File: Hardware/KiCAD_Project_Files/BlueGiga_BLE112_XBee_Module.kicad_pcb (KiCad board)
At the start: 4 copper layers, 24.5 x 24.4 mm, 11 parts, among them J2 HEADER_F_XBEE_PTH, P1 HEADER_2X5, U1 BLE112-A, U2 AAT3221

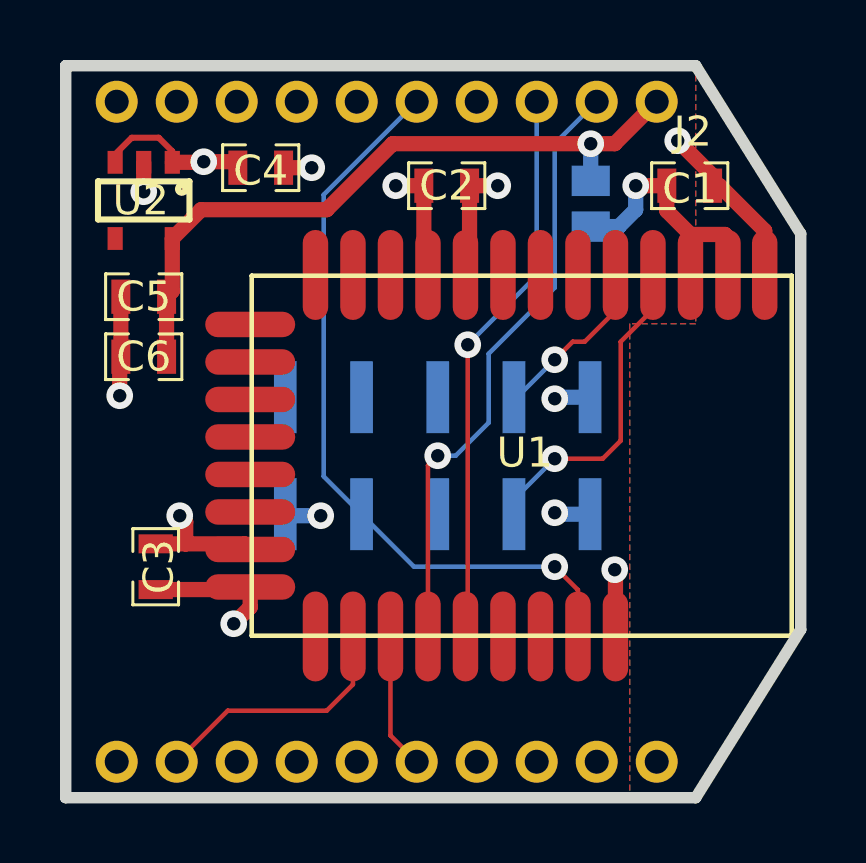
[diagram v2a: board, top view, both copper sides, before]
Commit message: Updated PCB layout to put 2mm pin header at same location as the RN-41XV. Added silkscreen artwork to back of PCB. Added assembly pdf drawings and schematic pdf. Added OSH Park PCB render images.
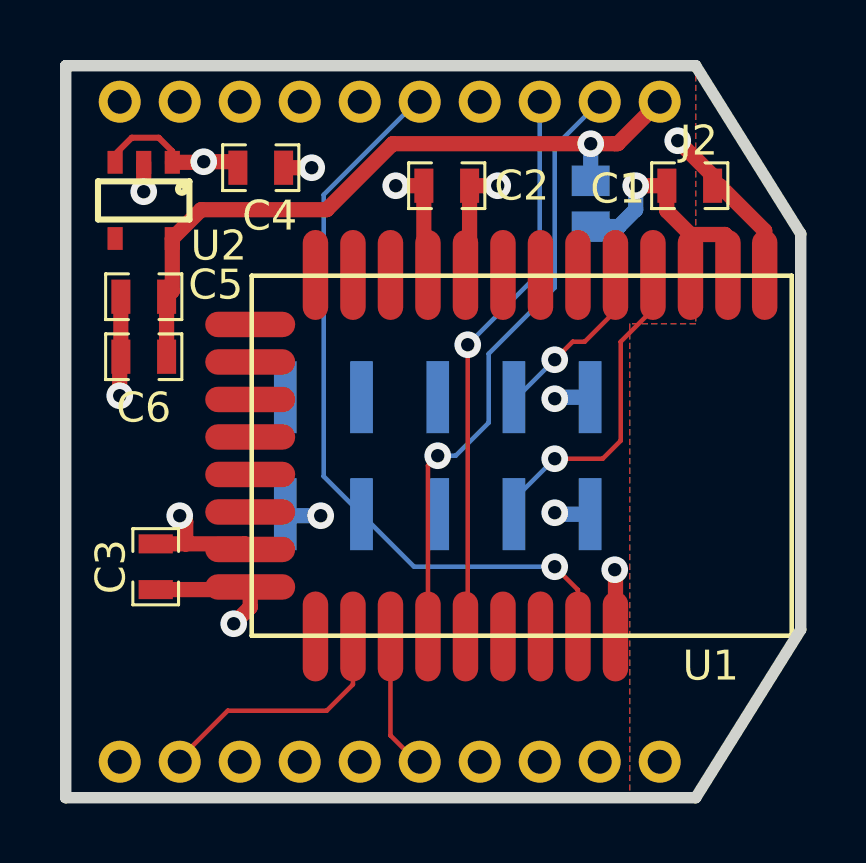
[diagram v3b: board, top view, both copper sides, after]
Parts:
- P1: value HEADER_2X5 -> (none)
- moved J2 0.10 mm to (118.8, 92.8)
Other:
- board text added: "BLE112"
- board text added: "REV 1"
- board text added: "www.cascologix.com"
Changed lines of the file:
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@@
     (links 36)
     (no_connects 0)
-    (area 85.517999 72.8948 126.3324 105.190501)
+    (area 98.809499 80.409499 123.690501 105.190501)
     (thickness 1.6002)
-    (drawings 8)
-    (tracks 124)
+    (drawings 11)
+    (tracks 128)
     (zones 0)
     (modules 11)
@@
   (module BLE112 locked (layer Front)
     (at 114.2 93.6 270)
-    (fp_text reference U1 (at -0.1 -0.1 360) (layer F.SilkS)
+    (fp_text reference U1 (at 7 -6.3 360) (layer F.SilkS)
       (effects (font (size 1 1) (thickness 0.1)))
     )
@@
     (at 119.8 84.6)
     (attr smd)
-    (fp_text reference C1 (at 0 0.1) (layer F.SilkS)
+    (fp_text reference C1 (at -2.4 0.1) (layer F.SilkS)
       (effects (font (size 1 1) (thickness 0.1)))
     )
@@
     (at 111.7 84.6 180)
     (attr smd)
-    (fp_text reference C2 (at 0 0 180) (layer F.SilkS)
+    (fp_text reference C2 (at -2.5 0 180) (layer F.SilkS)
       (effects (font (size 1 1) (thickness 0.1)))
     )
@@
     (at 102 97.3 270)
     (attr smd)
-    (fp_text reference C3 (at 0 -0.1 270) (layer F.SilkS)
+    (fp_text reference C3 (at 0 1.5 270) (layer F.SilkS)
       (effects (font (size 1 1) (thickness 0.1)))
     )
@@
     (at 105.5 84)
     (attr smd)
-    (fp_text reference C4 (at 0 0.1) (layer F.SilkS)
+    (fp_text reference C4 (at 0.3 1.6) (layer F.SilkS)
       (effects (font (size 1 1) (thickness 0.1)))
     )
@@
     (at 101.6 88.3 180)
     (attr smd)
-    (fp_text reference C5 (at 0 0 180) (layer F.SilkS)
+    (fp_text reference C5 (at -2.4 0.4 180) (layer F.SilkS)
       (effects (font (size 1 1) (thickness 0.1)))
     )
@@
     (at 101.6 90.3 180)
     (attr smd)
-    (fp_text reference C6 (at 0 0 180) (layer F.SilkS)
+    (fp_text reference C6 (at 0 -1.7 180) (layer F.SilkS)
       (effects (font (size 1 1) (thickness 0.1)))
     )
@@
   (module SOLDER_LINK (layer Back)
     (at 116.5 85.2)
-    (fp_text reference LK1 (at 0 0 270) (layer B.SilkS)
+    (fp_text reference LK1 (at -1.7 0 270) (layer B.SilkS)
       (effects (font (size 1 1) (thickness 0.1)) (justify mirror))
     )
@@
     (at 101.6 85.09 270)
     (attr smd)
-    (fp_text reference U2 (at 0 0.1 360) (layer F.SilkS)
+    (fp_text reference U2 (at 1.51 -2.5 360) (layer F.SilkS)
       (effects (font (size 1 1) (thickness 0.1)))
     )
@@
     )
   )
-  (module HEADER_XBEE locked (layer Front)
-    (at 118.7 92.8 270)
-    (fp_text reference J2 (at -10 -1.2 360) (layer F.SilkS)
+  (module HEADER_XBEE (layer Front)
+    (at 118.8 92.8 270)
+    (fp_text reference J2 (at -9.7 -1.3 540) (layer F.SilkS)
       (effects (font (size 1 1) (thickness 0.1)))
     )
@@
       (effects (font (size 1.016 1.016) (thickness 0.1524)) (justify mirror))
     )
-    (fp_text value HEADER_2X5 (at 0 5.08 180) (layer B.SilkS)
+    (fp_text value "" (at 0 5.08 180) (layer B.SilkS) hide
       (effects (font (size 1.016 1.016) (thickness 0.1524)) (justify mirror))
     )
@@
       (layers Back B.Paste B.Mask)
     )
+  )
+  (gr_text "REV 1" (at 101.3 93.1 270) (layer B.SilkS)
+    (effects (font (size 2.032 1.524) (thickness 0.3048)) (justify mirror))
+  )
+  (gr_text BLE112 (at 104.1 84.7) (layer B.SilkS)
+    (effects (font (size 2.032 1.524) (thickness 0.3048)) (justify mirror))
+  )
+  (gr_text www.cascologix.com (at 111.2 87.7) (layer B.SilkS)
+    (effects (font (size 2.032 1.524) (thickness 0.3048)) (justify mirror))
   )
   (dimension 24.4 (width 0.3048) (layer Dwgs.User)
@@
   (segment (start 112.462 87.438) (end 112.325 87.575) (width 0.508) (layer Front) (net 1))
   (segment (start 119.825 87.575) (end 119.825 86.225) (width 0.508) (layer Front) (net 1))
-  (segment (start 109.825 99.625) (end 109.825 102.925) (width 0.1524) (layer Front) (net 2))
-  (segment (start 109.825 102.925) (end 110.7 103.8) (width 0.1524) (layer Front) (net 2))
+  (segment (start 110.8 103.8) (end 110.7 103.8) (width 0.1524) (layer Front) (net 2))
+  (segment (start 109.825 102.925) (end 109.825 99.625) (width 0.1524) (layer Front) (net 2))
+  (segment (start 110.7 103.8) (end 109.825 102.925) (width 0.1524) (layer Front) (net 2))
   (segment (start 116.48 95.55) (end 115.35 95.55) (width 0.508) (layer Back) (net 3))
   (via (at 115.3 95.5) (size 0.889) (layers Front Back) (net 3))
@@
   (segment (start 117.5 93.1) (end 117.5 89.8) (width 0.1524) (layer Front) (net 5))
   (segment (start 116.9 93.7) (end 117.5 93.1) (width 0.1524) (layer Front) (net 5))
+  (segment (start 110.8 81.8) (end 110.7 81.8) (width 0.1524) (layer Back) (net 6))
+  (segment (start 107.6 94.29) (end 108.86 95.55) (width 0.1524) (layer Back) (net 6))
+  (segment (start 107.6 84.9) (end 107.6 94.29) (width 0.1524) (layer Back) (net 6))
+  (segment (start 110.7 81.8) (end 107.6 84.9) (width 0.1524) (layer Back) (net 6))
   (segment (start 108.86 95.55) (end 110.61 97.3) (width 0.1524) (layer Back) (net 6))
   (segment (start 116.075 98.075) (end 116.075 99.625) (width 0.1524) (layer Front) (net 6))
@@
   (via (at 115.3 97.3) (size 0.889) (layers Front Back) (net 6))
   (segment (start 110.61 97.3) (end 115.3 97.3) (width 0.1524) (layer Back) (net 6))
-  (segment (start 110.7 81.8) (end 107.6 84.9) (width 0.1524) (layer Back) (net 6))
-  (segment (start 107.6 94.29) (end 108.86 95.55) (width 0.1524) (layer Back) (net 6))
-  (segment (start 107.6 84.9) (end 107.6 94.29) (width 0.1524) (layer Back) (net 6))
   (segment (start 108.86 95.55) (end 108.95 95.55) (width 0.1524) (layer Back) (net 6))
-  (segment (start 108.575 99.625) (end 108.575 101.225) (width 0.1524) (layer Front) (net 7))
-  (segment (start 104.4 102.1) (end 102.7 103.8) (width 0.1524) (layer Front) (net 7))
+  (segment (start 102.8 103.8) (end 102.8 103.7) (width 0.1524) (layer Front) (net 7))
+  (segment (start 108.575 101.225) (end 107.7 102.1) (width 0.1524) (layer Front) (net 7))
   (segment (start 107.7 102.1) (end 104.4 102.1) (width 0.1524) (layer Front) (net 7))
-  (segment (start 108.575 101.225) (end 107.7 102.1) (width 0.1524) (layer Front) (net 7))
+  (segment (start 108.575 101.225) (end 108.575 99.625) (width 0.1524) (layer Front) (net 7))
+  (segment (start 102.8 103.7) (end 104.4 102.1) (width 0.1524) (layer Front) (net 7))
+  (segment (start 114.7 87.6) (end 114.8 87.5) (width 0.1524) (layer Back) (net 8))
+  (segment (start 112.325 99.625) (end 112.4 99.55) (width 0.1524) (layer Front) (net 8))
+  (segment (start 112.4 89.9) (end 112.4 99.55) (width 0.1524) (layer Front) (net 8))
+  (via (at 112.4 89.9) (size 0.889) (layers Front Back) (net 8))
   (segment (start 112.4 89.9) (end 114.7 87.6) (width 0.1524) (layer Back) (net 8))
-  (via (at 112.4 89.9) (size 0.889) (layers Front Back) (net 8))
-  (segment (start 112.4 89.9) (end 112.4 99.55) (width 0.1524) (layer Front) (net 8))
-  (segment (start 112.325 99.625) (end 112.4 99.55) (width 0.1524) (layer Front) (net 8))
-  (segment (start 114.7 87.6) (end 114.7 81.8) (width 0.1524) (layer Back) (net 8))
+  (segment (start 114.8 87.5) (end 114.8 81.8) (width 0.1524) (layer Back) (net 8))
+  (segment (start 116.8 81.8) (end 115.3 83.3) (width 0.1524) (layer Back) (net 9))
   (segment (start 115.3 88) (end 113.1 90.2) (width 0.1524) (layer Back) (net 9))
-  (segment (start 116.7 81.8) (end 115.3 83.2) (width 0.1524) (layer Back) (net 9))
-  (segment (start 115.3 83.2) (end 115.3 88) (width 0.1524) (layer Back) (net 9))
+  (segment (start 115.3 83.3) (end 115.3 88) (width 0.1524) (layer Back) (net 9))
   (segment (start 111.075 93.925) (end 111.075 99.625) (width 0.1524) (layer Front) (net 9))
   (segment (start 111.4 93.6) (end 111.075 93.925) (width 0.1524) (layer Front) (net 9))
@@
   (segment (start 113.1 92.5) (end 112 93.6) (width 0.1524) (layer Back) (net 9))
   (segment (start 113.1 90.2) (end 113.1 92.5) (width 0.1524) (layer Back) (net 9))
+  (segment (start 118.8 81.8) (end 117.4 83.2) (width 0.508) (layer Front) (net 10))
+  (segment (start 117.3 83.2) (end 116.5 83.2) (width 0.508) (layer Front) (net 10))
+  (segment (start 117.3 83.2) (end 117.4 83.2) (width 0.508) (layer Front) (net 10))
   (segment (start 116.5 84.438) (end 116.5 83.2) (width 0.508) (layer Back) (net 10))
   (via (at 116.5 83.2) (size 0.889) (layers Front Back) (net 10))
-  (segment (start 118.7 81.8) (end 118.7 81.8) (width 0.508) (layer Front) (net 10))
   (segment (start 103.5125 85.4) (end 102.5525 86.36) (width 0.508) (layer Front) (net 10))
   (segment (start 107.7 85.4) (end 103.5125 85.4) (width 0.508) (layer Front) (net 10))
   (segment (start 109.9 83.2) (end 107.7 85.4) (width 0.508) (layer Front) (net 10))
-  (segment (start 117.3 83.2) (end 116.5 83.2) (width 0.508) (layer Front) (net 10))
   (segment (start 116.5 83.2) (end 109.9 83.2) (width 0.508) (layer Front) (net 10))
-  (segment (start 118.7 81.8) (end 117.3 83.2) (width 0.508) (layer Front) (net 10))
   (segment (start 102.362 90.3) (end 102.362 88.3) (width 0.508) (layer Front) (net 10))
   (segment (start 102.5525 86.36) (end 102.5525 88.1095) (width 0.508) (layer Front) (net 10))

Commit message: Fixed debugger connector, added renders, updated board drawings with layout changes and rev and date.
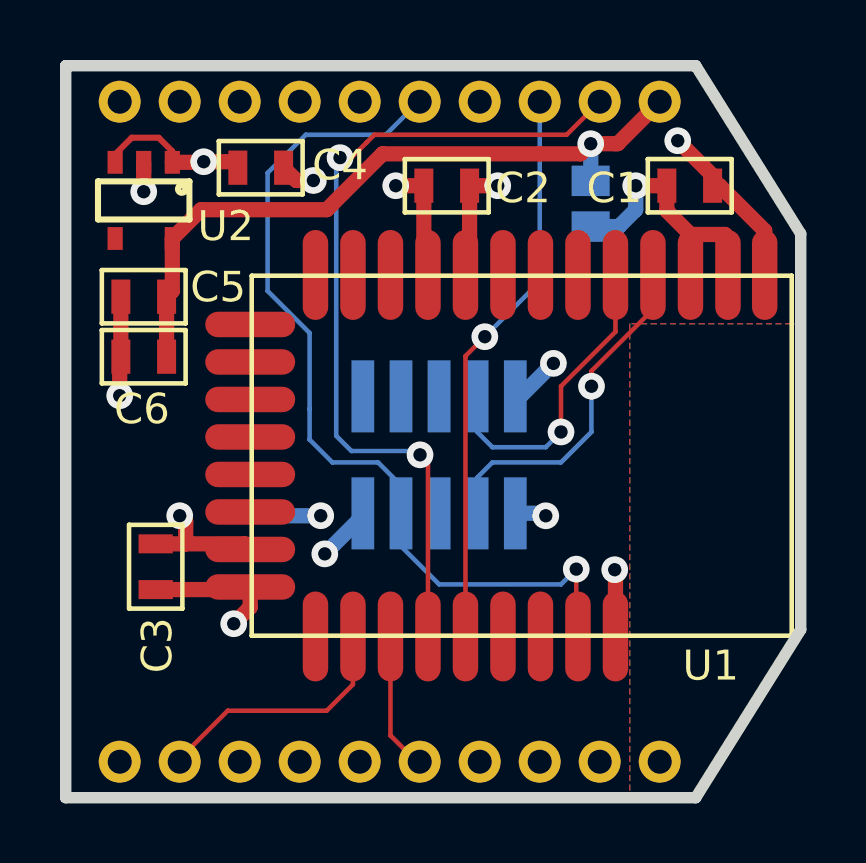
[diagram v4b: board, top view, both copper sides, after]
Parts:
- C1, C2, C3, C4, C5, C6: footprint 0603 -> C0603
- J2: moved to B.Cu
- P1: value (none) -> HEADER_2X5
- moved P1 0.05 mm to (111.4, 93.6)
- turned J2 to 90 degrees
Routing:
- net TX: track 20.5 -> 28.0 mm, vias 1 -> 2
- net P2_1: track 5.78 -> 10.4 mm
- net RESET: track 25.6 -> 30.1 mm
- net +3.3V: track 28.0 -> 29.2 mm
- net (no net): track 0.00 -> 1.20 mm, vias 0 -> 1
- net P2_2: track 10.8 -> 11.7 mm
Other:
- board text added: "REV 2"
- board text removed: "REV 1"

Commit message: Simplified design into a 3.3V-only.  A branch has been started to continue to support potential dual voltage (3.3V & 5V) designs.
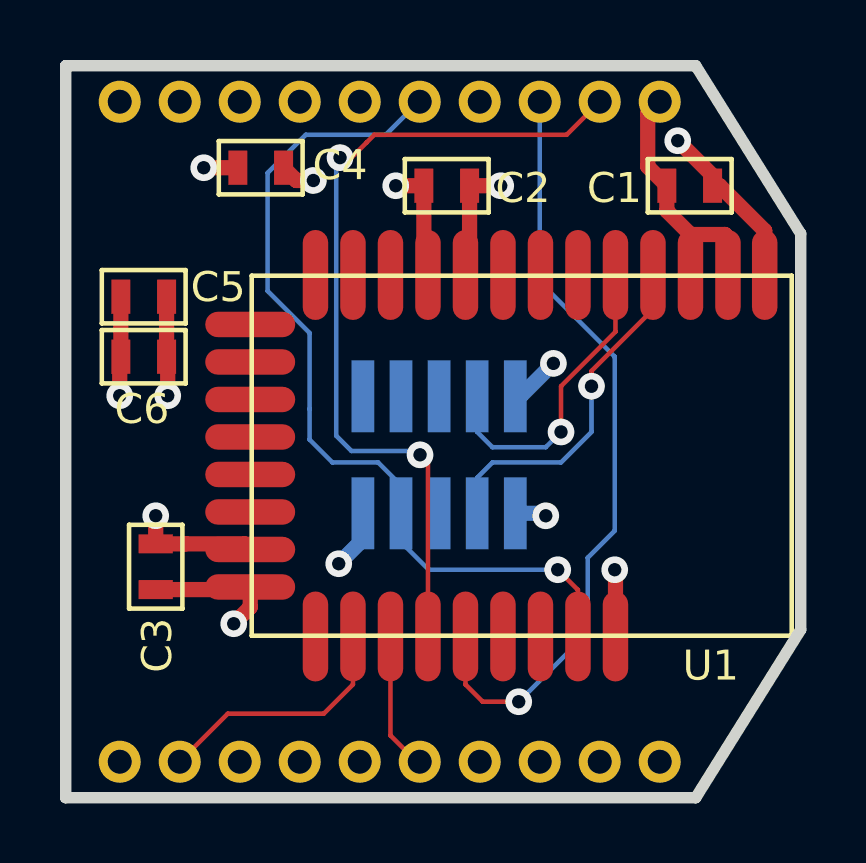
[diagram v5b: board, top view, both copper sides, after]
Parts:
- removed LK1: SOLDER_LINK, SOLDER_LINK
- removed U2: AAT3221, SOT23-5_SMT
- C4, C5: value 2.2u -> 4.7u
- P1: renamed from J2; value HEADER_F_XBEE_PTH -> XBEE HEADER
- P2: renamed from P1; value HEADER_2X5 -> DEBUG
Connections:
- C1 pad 1: +3.3V -> +3V3
- C2 pad 1: +3.3V -> +3V3
- C3 pad 1: +3.3V -> +3V3
- C4 pad 1: +3.3V -> +3V3
- C5 pad 1: VCC -> +3V3
- C6 pad 1: VCC -> +3V3
- P1 pad 1: VCC -> +3V3
- P1 pad 11: (no net) -> Net-(P1-Pad11)
- P1 pad 13: (no net) -> Net-(P1-Pad13)
- P1 pad 14: (no net) -> Net-(P1-Pad14)
- P1 pad 15: (no net) -> Net-(P1-Pad15)
- P1 pad 17: (no net) -> Net-(P1-Pad17)
- P1 pad 18: (no net) -> Net-(P1-Pad18)
- P1 pad 19: (no net) -> Net-(P1-Pad19)
- P1 pad 20: (no net) -> Net-(P1-Pad20)
- P1 pad 4: (no net) -> Net-(P1-Pad4)
- P1 pad 6: (no net) -> Net-(P1-Pad6)
- P1 pad 7: (no net) -> Net-(P1-Pad7)
- P1 pad 8: (no net) -> Net-(P1-Pad8)
- P1 pad 9: (no net) -> Net-(P1-Pad9)
- P2 pad 10: (no net) -> Net-(P2-Pad10)
- P2 pad 2: +3.3V -> +3V3
- P2 pad 5: (no net) -> Net-(P2-Pad5)
- P2 pad 6: (no net) -> Net-(P2-Pad6)
- P2 pad 8: (no net) -> Net-(P2-Pad8)
- P2 pad 9: +3.3V -> +3V3
- U1 pad 11: (no net) -> Net-(U1-Pad11)
- U1 pad 12: (no net) -> Net-(U1-Pad12)
- U1 pad 13: (no net) -> Net-(U1-Pad13)
- U1 pad 14: (no net) -> Net-(U1-Pad14)
- U1 pad 15: (no net) -> Net-(U1-Pad15)
- U1 pad 16: (no net) -> Net-(U1-Pad16)
- U1 pad 17: (no net) -> Net-(U1-Pad17)
- U1 pad 18: (no net) -> Net-(U1-Pad18)
- U1 pad 19: (no net) -> Net-(U1-Pad19)
- U1 pad 2: +3.3V -> +3V3
- U1 pad 20: +3.3V -> +3V3
- U1 pad 22: (no net) -> Net-(U1-Pad22)
- U1 pad 27: (no net) -> Net-(U1-Pad27)
- U1 pad 28: (no net) -> Net-(U1-Pad28)
- U1 pad 3: +3.3V -> +3V3
- U1 pad 6: (no net) -> Net-(U1-Pad6)
- U1 pad 7: (no net) -> Net-(U1-Pad7)
- U1 pad 8: (no net) -> Net-(U1-Pad8)
- U1 pad 9: +3.3V -> +3V3
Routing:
- net +3.3V: track 29.2 -> 0.00 mm, vias 6 -> 0
- net +3V3: track 0.00 -> 28.3 mm, vias 0 -> 6
- net VCC: track 23.4 -> 0.00 mm, vias 1 -> 0
- net RX: track 18.9 -> 26.0 mm
- net (no net): track 1.20 -> 0.00 mm, vias 1 -> 0
- net GND: track 23.2 -> 22.2 mm, vias 8 -> 7
- added copper zone on Inner2-Pwr.Cu, net +3V3
- removed copper zone on B.Cu, net (none)
- removed copper zone on F.Cu, net (none)
- removed copper zone on Inner2-Pwr.Cu, net +3.3V
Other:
- board text added: "REV 4"
- board text removed: "REV 2"
